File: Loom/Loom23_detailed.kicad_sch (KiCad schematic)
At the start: 7 parts

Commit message: Reorganized Loom folder
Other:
- removed sheet Cooling fan (rear)
- removed sheet Engine speed sensor
- removed sheet Oil pressure sensor
- added sheet Telemetry (Telemetry/telemetry_board.kicad_sch)
- sheet BPS: file BPS.kicad_sch -> Brake System Plausability Device/brake_pressure_sensor.kicad_sch
- sheet BSPD: file BSPD.kicad_sch -> Brake System Plausability Device/BSPD.kicad_sch
- sheet Cam sensor: file CamSensor.kicad_sch -> Engine Sensors/cam_sensor.kicad_sch
- sheet Coolant temperature sensor: file CLT.kicad_sch -> Engine Sensors/coolant_temperature.kicad_sch
- sheet Cooling fan (left): file CoolingFan.kicad_sch -> Engine/cooling_fan.kicad_sch
- sheet Cooling fan (right): file CoolingFan.kicad_sch -> Engine/cooling_fan.kicad_sch
- sheet Crank sensor: file crankSensor.kicad_sch -> Engine Sensors/crank_sensor.kicad_sch
- sheet Dash Arduino and screen: file Dash Arduino.kicad_sch -> Dash/dash_switches.kicad_sch
- sheet Dash Break-out-board: file DashBoB.kicad_sch -> Dash/dash_break_out_board.kicad_sch
- sheet Dash switches: file Dash switches.kicad_sch -> Dash/dash_switches.kicad_sch
- sheet ECU: file ECU.kicad_sch -> ECU/ECU.kicad_sch
- sheet Fuel Pump: file fuelPump.kicad_sch -> Engine/fuel_pump.kicad_sch
- sheet Fusebox: file Fusebox.kicad_sch -> Power/fusebox.kicad_sch
- sheet Gearbox pneumatics: file Gearbox pneumatics.kicad_sch -> Paddle shifter/gearbox_pneumatics.kicad_sch
- sheet Ignition: file ignition.kicad_sch -> Engine/ignition.kicad_sch
- sheet Injector1: file Injector.kicad_sch -> Engine/injector.kicad_sch
- sheet Injector2: file Injector.kicad_sch -> Engine/injector.kicad_sch
- sheet Injector3: file Injector.kicad_sch -> Engine/injector.kicad_sch
- sheet Injector4: file Injector.kicad_sch -> Engine/injector.kicad_sch
- sheet Intake air temperature: file IAT.kicad_sch -> Engine Sensors/intake_air_temperature.kicad_sch
- sheet Lambda sensor: file Lambda.kicad_sch -> Engine Sensors/lambda_sensor.kicad_sch
- sheet Manifold absolute pressure: file MAP.kicad_sch -> Engine Sensors/manifold_air_pressure.kicad_sch
- sheet Paddle shifters: file Paddle shifters.kicad_sch -> Paddle shifter/paddle_shifters.kicad_sch
- sheet RPM LEDs and wheel buttons: file RPM LEDs.kicad_sch -> Dash/RPM_LEDs.kicad_sch
- sheet Relaybox: file Relaybox.kicad_sch -> Power/relaybox.kicad_sch
- sheet Starter motor: file Starter motor.kicad_sch -> Engine/starter_motor.kicad_sch
- sheet Starter relay: file Starter relay and switch.kicad_sch -> Engine/starter_relay.kicad_sch
- sheet TPS (BSPD): file TPS(BSPD).kicad_sch -> Brake System Plausability Device/throttle_position_sensor_bspd.kicad_sch
- sheet Throttle position sensor (ECU): file TPS (ECU).kicad_sch -> Engine Sensors/throttle_position_sensor_ecu.kicad_sch

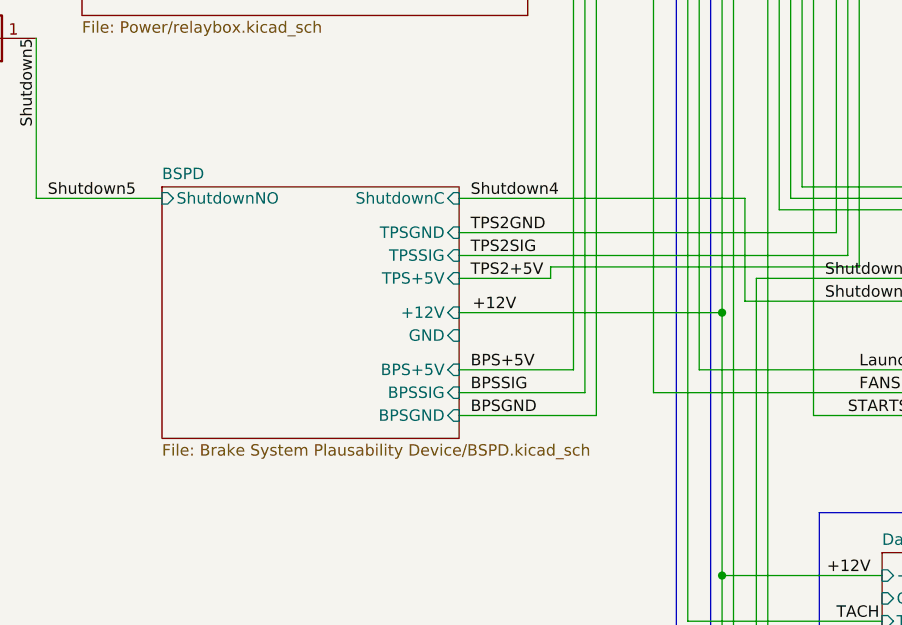
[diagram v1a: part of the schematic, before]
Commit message: Update Loom Schematic with New BSPD
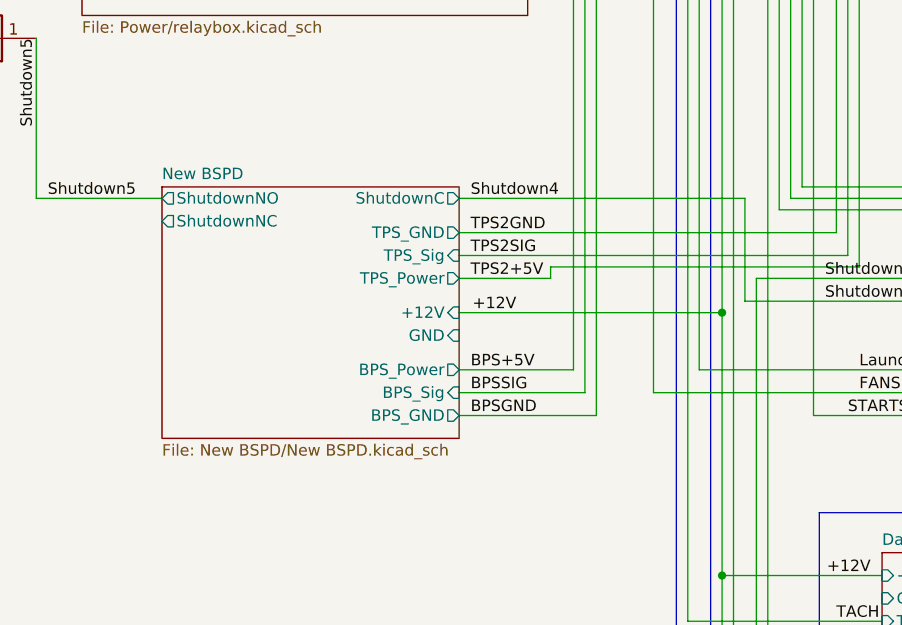
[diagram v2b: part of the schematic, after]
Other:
- removed sheet BSPD
- added sheet New BSPD (New BSPD/New BSPD.kicad_sch)
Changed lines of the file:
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@@
-    )
-  )
-  (sheet (at 171.45 173.99) (size 33.02 27.94) (fields_autoplaced)
-    (stroke (width 0.1524) (type solid))
-    (fill (color 0 0 0 0.0000))
-    (property "Sheetname" "BSPD" (at 171.45 173.2784 0)
-      (effects (font (size 1.27 1.27)) (justify left bottom))
-    )
-    (property "Sheetfile" "Brake System Plausability Device/BSPD.kicad_sch" (at 171.45 202.5146 0)
-      (effects (font (size 1.27 1.27)) (justify left top))
-    )
-    (pin "GND" input (at 204.47 190.5 0)
-      (effects (font (size 1.27 1.27)) (justify right))
-    )
-    (pin "+12V" input (at 204.47 187.96 0)
-      (effects (font (size 1.27 1.27)) (justify right))
-    )
-    (pin "BPS+5V" input (at 204.47 194.31 0)
-      (effects (font (size 1.27 1.27)) (justify right))
-    )
-    (pin "BPSSIG" input (at 204.47 196.85 0)
-      (effects (font (size 1.27 1.27)) (justify right))
-    )
-    (pin "BPSGND" input (at 204.47 199.39 0)
-      (effects (font (size 1.27 1.27)) (justify right))
-    )
-    (pin "TPSGND" input (at 204.47 179.07 0)
-      (effects (font (size 1.27 1.27)) (justify right))
-    )
-    (pin "TPSSIG" input (at 204.47 181.61 0)
-      (effects (font (size 1.27 1.27)) (justify right))
-    )
-    (pin "TPS+5V" input (at 204.47 184.15 0)
-      (effects (font (size 1.27 1.27)) (justify right))
-    )
-    (pin "ShutdownNO" input (at 171.45 175.26 180)
-      (effects (font (size 1.27 1.27)) (justify left))
-    )
-    (pin "ShutdownC" input (at 204.47 175.26 0)
-      (effects (font (size 1.27 1.27)) (justify right))
-    )
-    (instances
-      (project "Loom23_detailed"
-        (path "/691c98c8-9b47-40a5-87b6-2865e3f6892d" (page "18"))
-      )
     )
   )
@@
       )
     )
+  )
+  (sheet (at 171.45 173.99) (size 33.02 27.94) (fields_autoplaced)
+    (stroke (width 0.1524) (type solid))
+    (fill (color 0 0 0 0.0000))
+    (property "Sheetname" "New BSPD" (at 171.45 173.2784 0)
+      (effects (font (size 1.27 1.27)) (justify left bottom))
+    )
+    (property "Sheetfile" "New BSPD/New BSPD.kicad_sch" (at 171.45 202.5146 0)
+      (effects (font (size 1.27 1.27)) (justify left top))
+    )
+    (pin "TPS_Power" output (at 204.47 184.15 0)
+      (effects (font (size 1.27 1.27)) (justify right))
+    )
+    (pin "TPS_Sig" input (at 204.47 181.61 0)
+      (effects (font (size 1.27 1.27)) (justify right))
+    )
+    (pin "BPS_Sig" input (at 204.47 196.85 0)
+      (effects (font (size 1.27 1.27)) (justify right))
+    )
+    (pin "BPS_GND" output (at 204.47 199.39 0)
+      (effects (font (size 1.27 1.27)) (justify right))
+    )
+    (pin "BPS_Power" output (at 204.47 194.31 0)
+      (effects (font (size 1.27 1.27)) (justify right))
+    )
+    (pin "ShutdownNO" output (at 171.45 175.26 180)
+      (effects (font (size 1.27 1.27)) (justify left))
+    )
+    (pin "ShutdownNC" output (at 171.45 177.8 180)
+      (effects (font (size 1.27 1.27)) (justify left))
+    )
+    (pin "ShutdownC" output (at 204.47 175.26 0)
+      (effects (font (size 1.27 1.27)) (justify right))
+    )
+    (pin "TPS_GND" output (at 204.47 179.07 0)
+      (effects (font (size 1.27 1.27)) (justify right))
+    )
+    (pin "GND" input (at 204.47 190.5 0)
+      (effects (font (size 1.27 1.27)) (justify right))
+    )
+    (pin "+12V" input (at 204.47 187.96 0)
+      (effects (font (size 1.27 1.27)) (justify right))
+    )
+    (instances
+      (project "Loom23_detailed"
+        (path "/691c98c8-9b47-40a5-87b6-2865e3f6892d" (page "33"))
+      )
+    )
